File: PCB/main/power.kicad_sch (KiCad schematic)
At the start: 22 parts, among them J1 USB_B_Micro, Q1 IRF9540NPbF, U1 MCP73831-2-OT, U2 FT232RL, U3 MCP1700-3302E_TO92

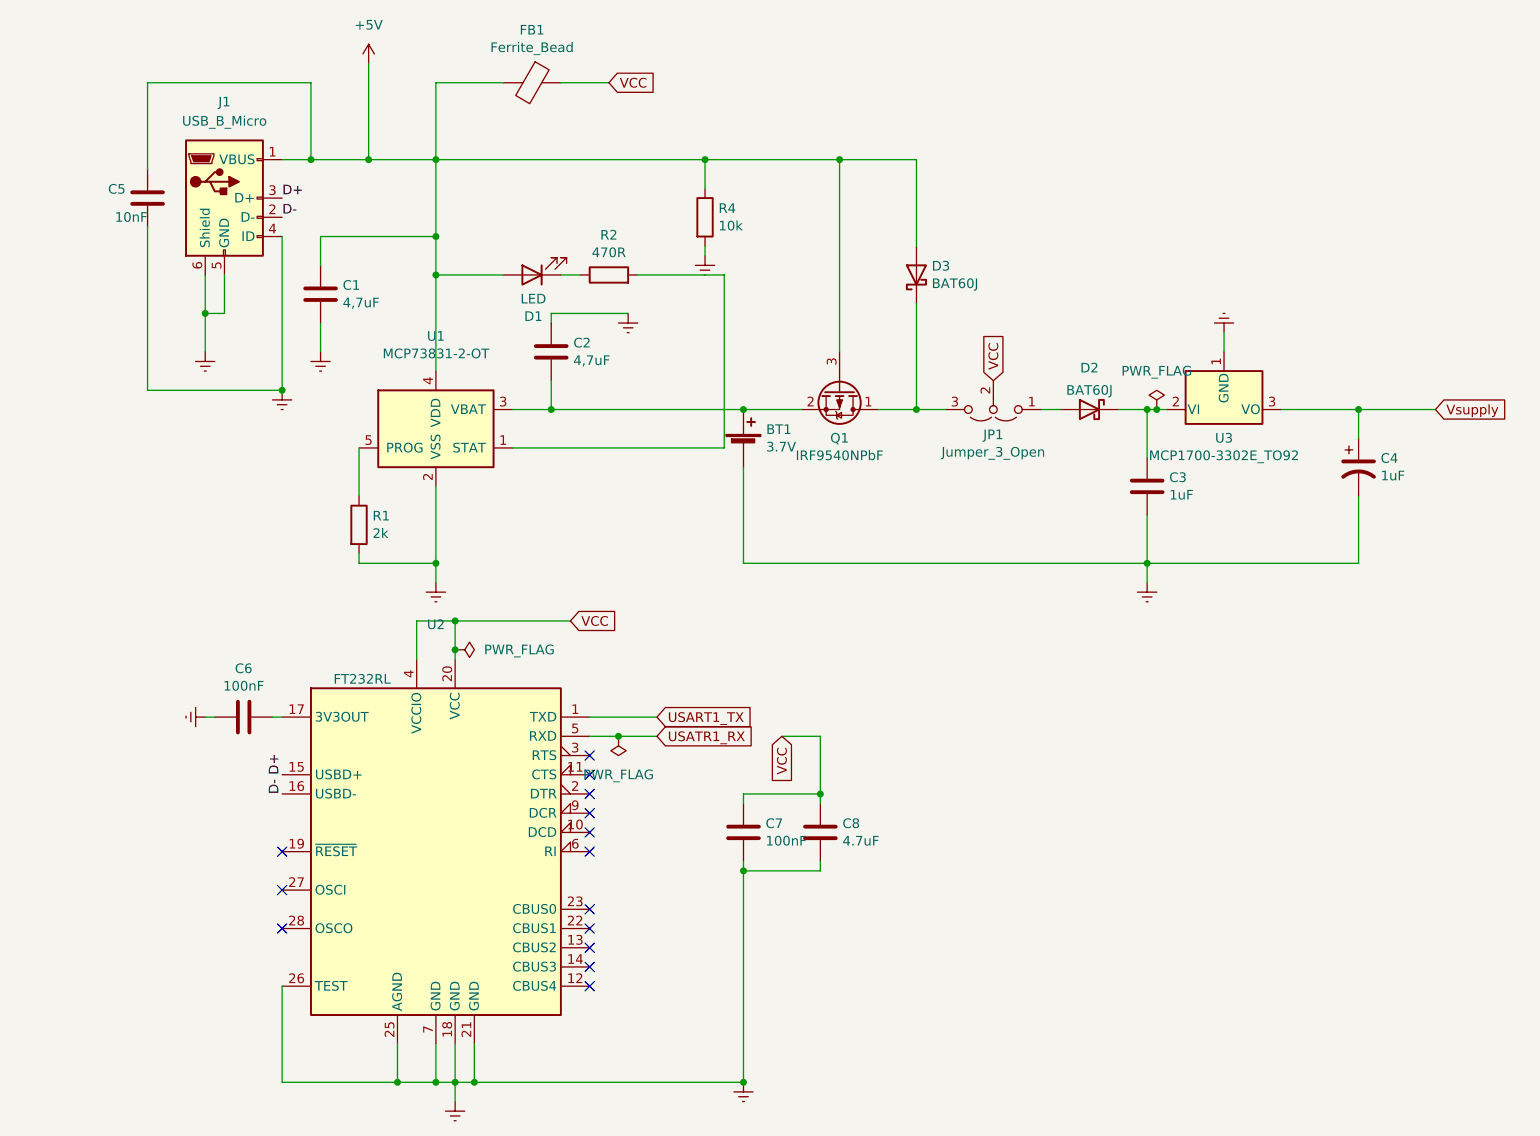
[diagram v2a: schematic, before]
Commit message: power and microcontroller updated
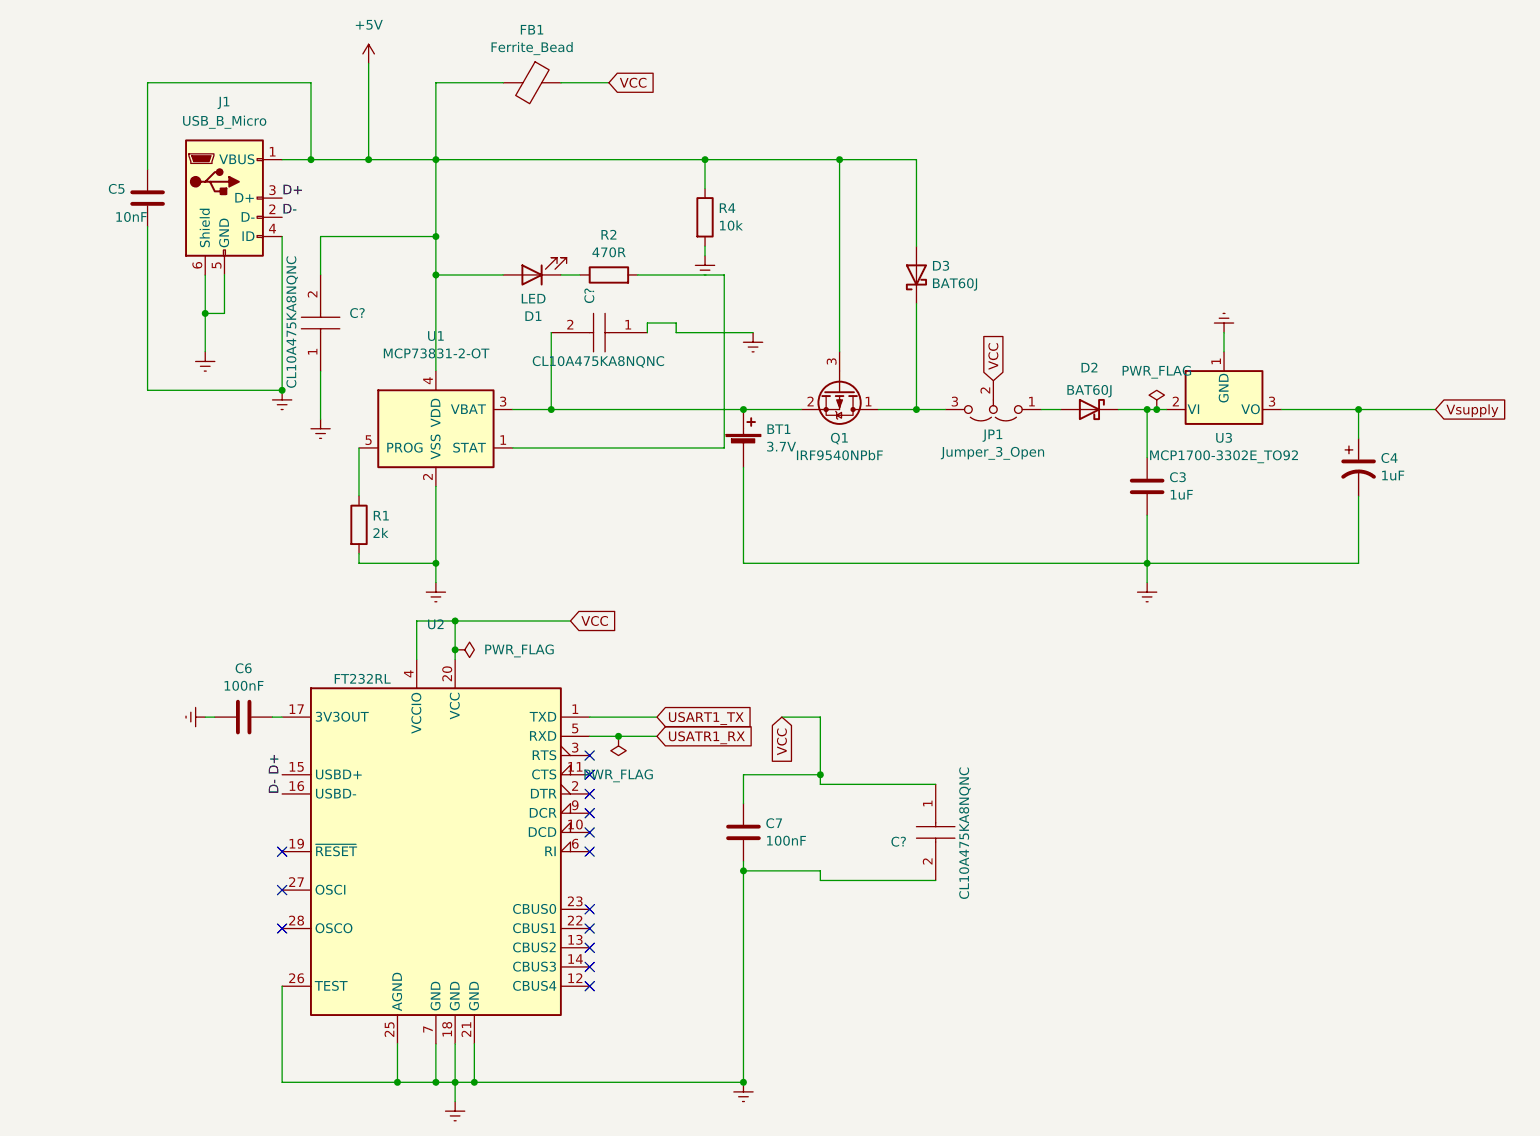
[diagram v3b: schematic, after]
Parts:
- removed C1, C2: 4,7uF, SamacSys_Parts:CAPC1608X90N, symbol Device:C
- removed C8: 4.7uF, SamacSys_Parts:CAPC1608X90N, symbol Device:C
- added C? (x3): CL10A475KA8NQNC, CAPC1608X95N, symbol SamacSys_Parts_Microcontroller:CL10A475KA8NQNC
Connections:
- net +5V: now also C?.2
- net Earth: now also C?.1, C?.1, C?.2
- net VCC: now also C?.1
- net at BT1.1 (+), Q1.2 (S), U1.3 (VBAT): now also C?.2

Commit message: changes made to all
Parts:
- removed R2: 470R, SamacSys_Parts:RESC1608X55N, symbol Device:R
- added R2: RC0805FR-07470RL, RESC2012X60N, symbol SamacSys_Parts_Microcontroller:RC0805FR-07470RL
- gave numbers to parts that had none: 3
- renumbered C5 to C1, C6 to C2, C7 to C5, C3 to C7, C4 to C8, D3 to D2, D2 to D3, J1 to J5, R4 to R3
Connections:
- net at U1.1 (STAT): now also R2.2
- net at D1.1 (K): now also R2.1
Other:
- moved on the sheet: D1

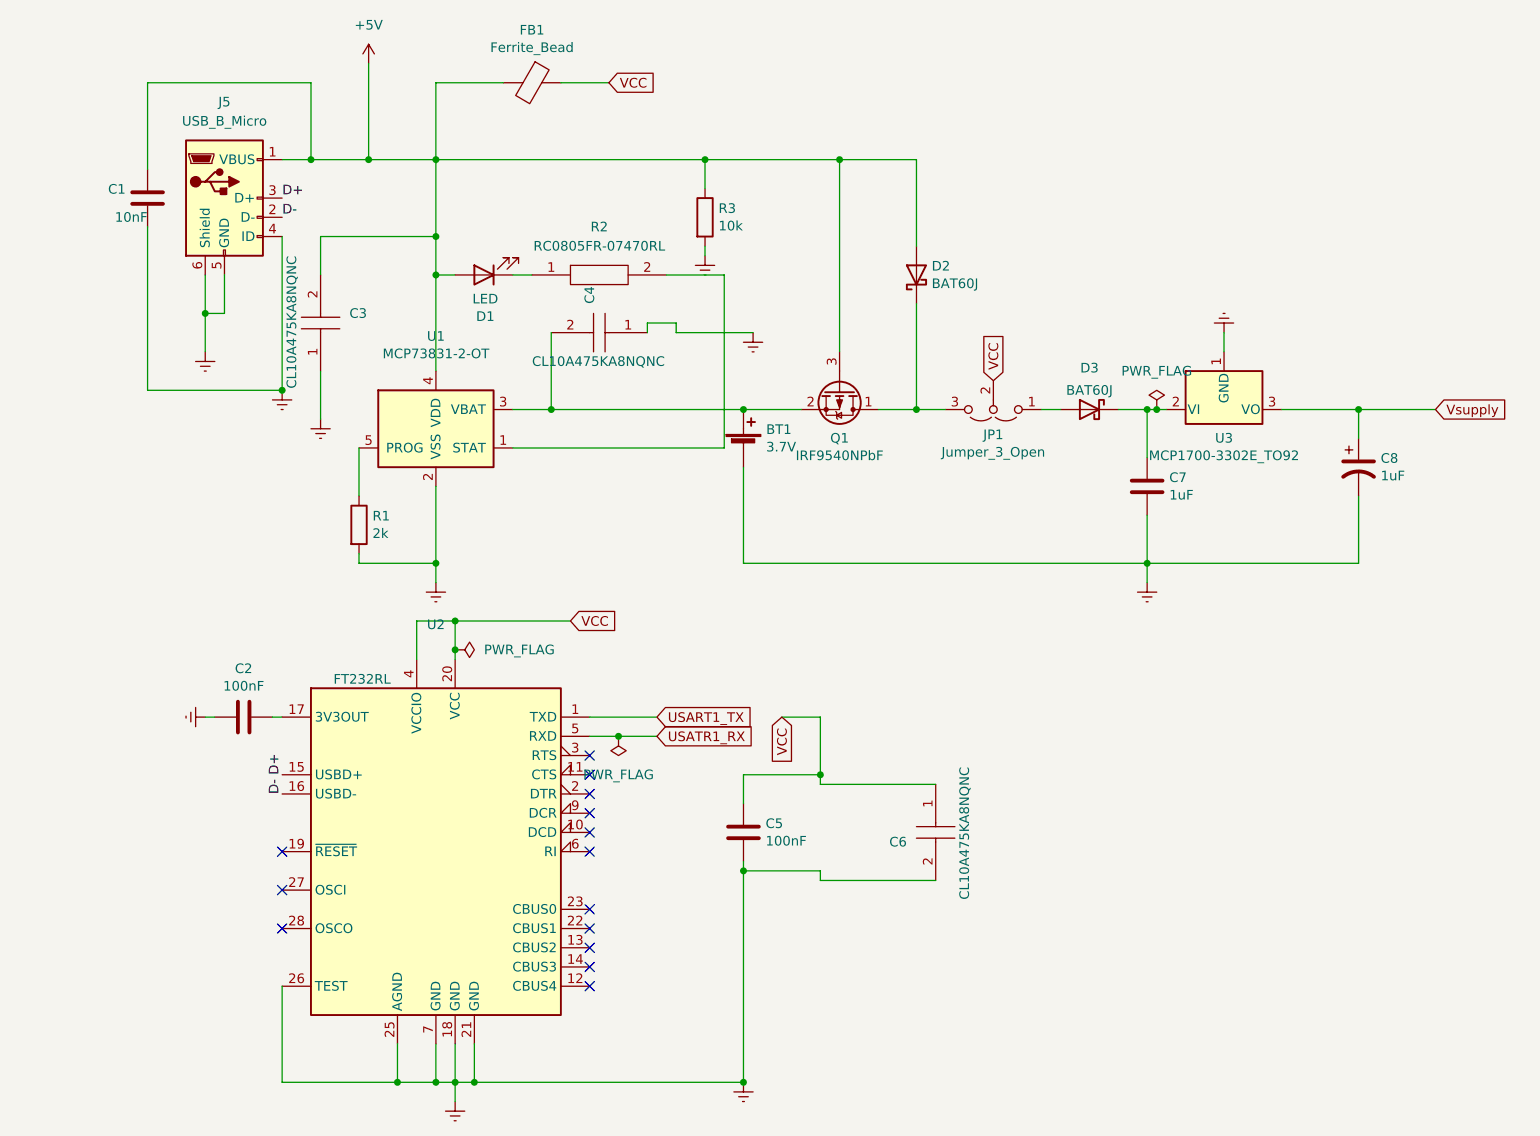
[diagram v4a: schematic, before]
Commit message: changed USB MICRO
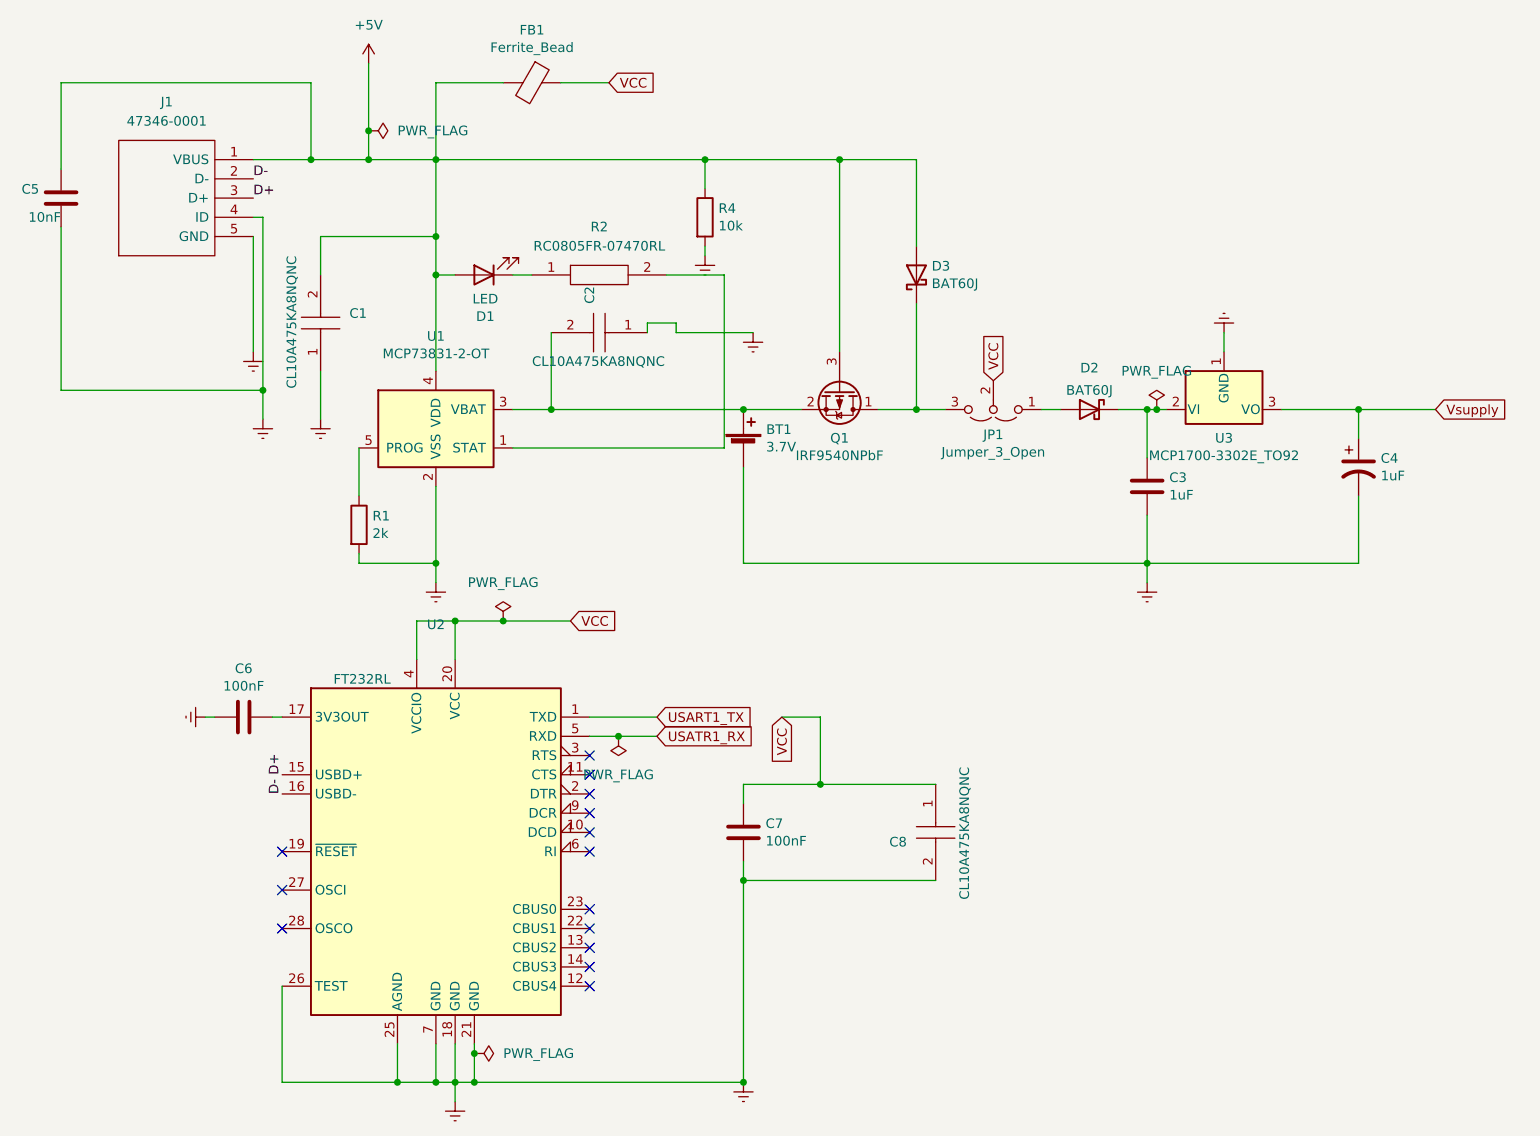
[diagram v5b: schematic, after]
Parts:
- removed J5: USB_B_Micro, SamacSys_Parts:MICROXNJ, symbol Connector:USB_B_Micro
- added J1: 47346-0001, SamacSys_Parts:47346-0001, symbol SamaSys_Parts:47346-0001
- renumbered C3 to C1, C4 to C2, C7 to C3, C8 to C4, C1 to C5, C2 to C6, C5 to C7, C6 to C8, D3 to D2, D2 to D3, R3 to R4
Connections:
- net +5V: now also J1.1 (VBUS)
- net D+: now also J1.3 (D+)
- net D-: now also J1.2 (D-)
- net Earth: now also J1.4 (ID), J1.5 (GND)
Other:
- moved on the sheet: C5
